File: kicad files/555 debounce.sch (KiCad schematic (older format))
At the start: 7 parts, among them SW1 SW_PUSH_BUTTON

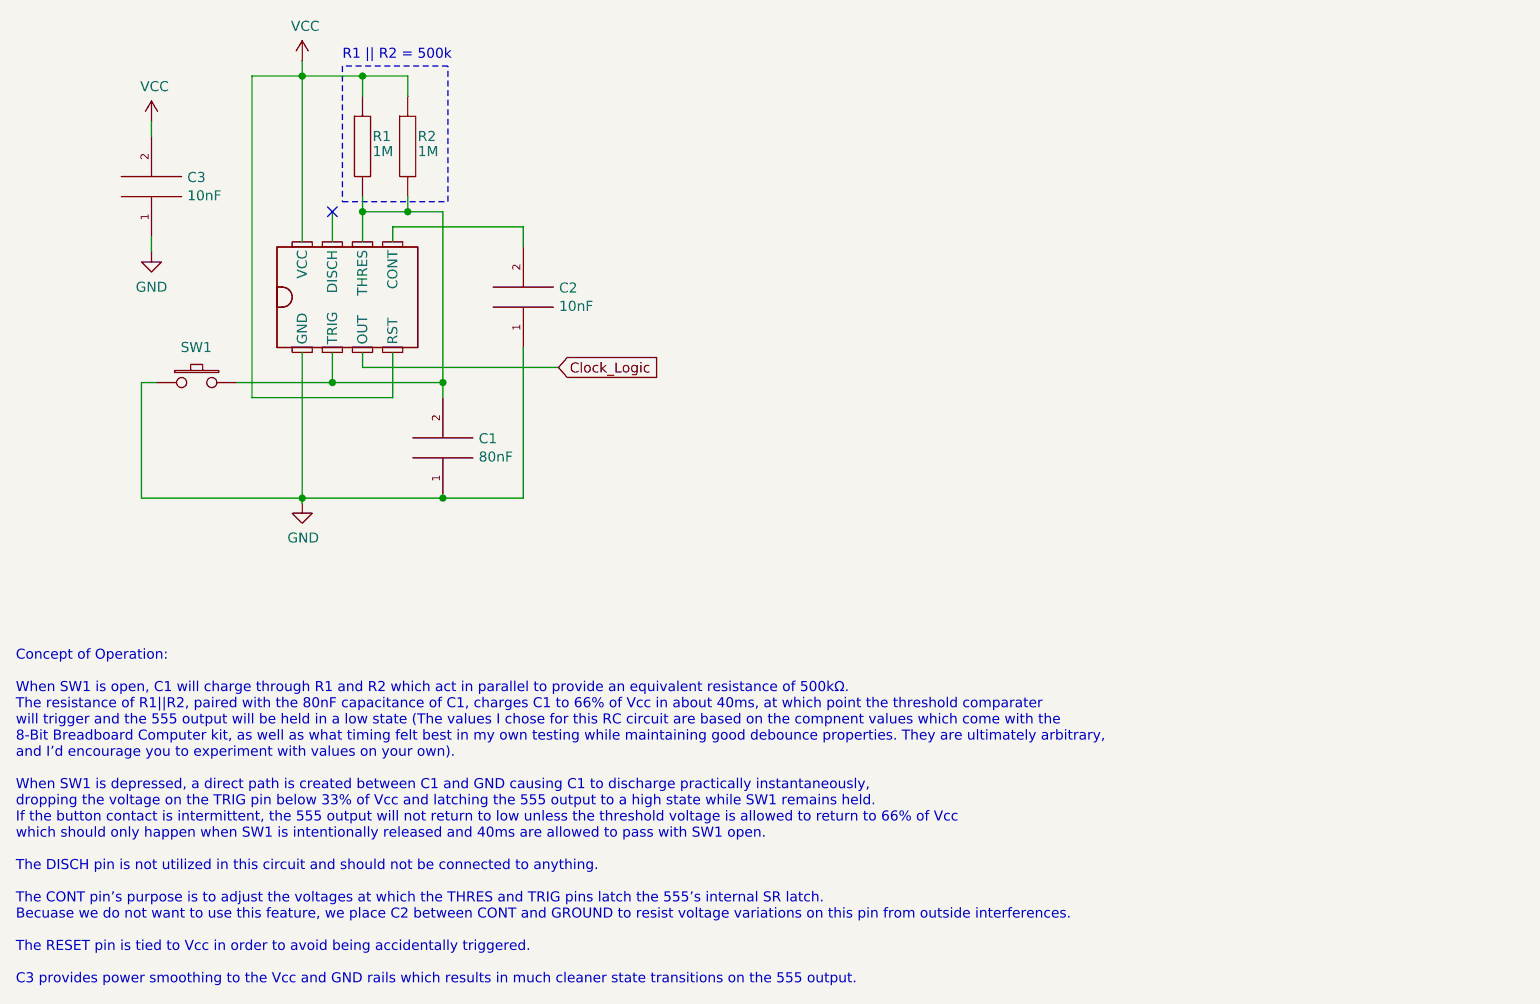
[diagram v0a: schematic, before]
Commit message: corrected C2 value and minor edits
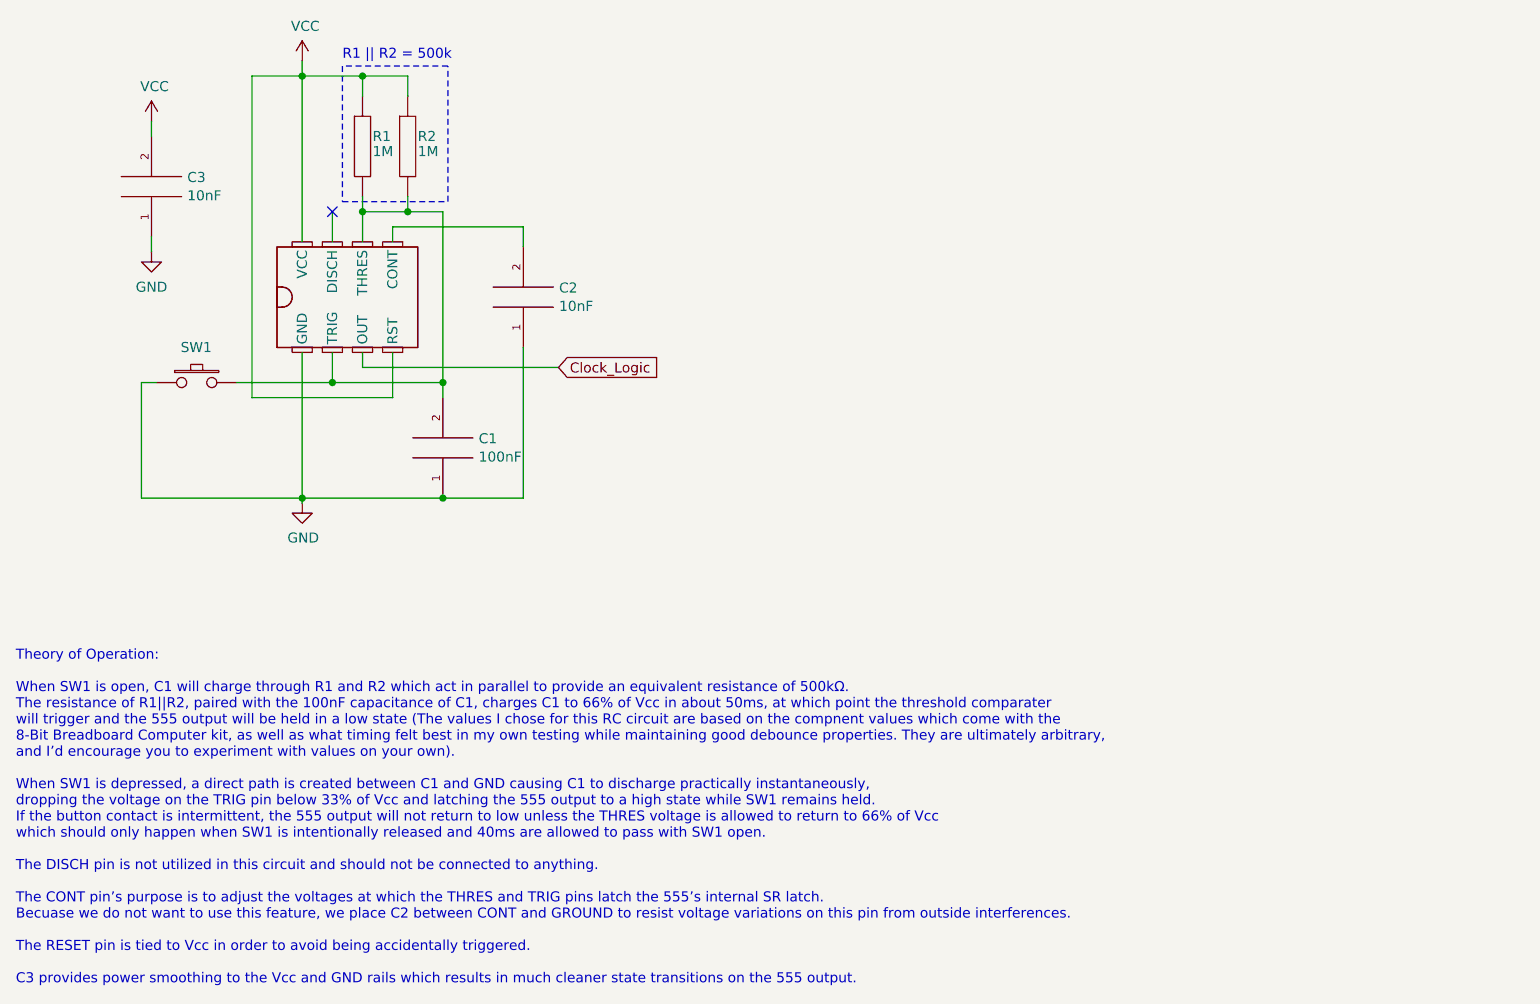
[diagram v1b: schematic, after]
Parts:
- C1: value 80nF -> 100nF
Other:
- note added: "Theory of Operation:\n\nWhen SW1 is open, C1 will charge through R1 and R2 which act in parallel to provide an equivalent resistance of 500kΩ. \nThe resistance of R1||R2, paired with the 100nF capacitance of C1, charges C1 to 66% of Vcc in about 50ms, at which point the threshold comparater \nwill trigger and the 555 output will be held in a low state (The values I chose for this RC circuit are b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"
- note removed: "Concept of Operation:\n\nWhen SW1 is open, C1 will charge through R1 and R2 which act in parallel to provide an equivalent resistance of 500kΩ. \nThe resistance of R1||R2, paired with the 80nF capacitance of C1, charges C1 to 66% of Vcc in about 40ms, at which point the threshold comparater \nwill trigger and the 555 output will be held in a low state (The values I chose for this RC circuit are b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"
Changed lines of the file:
@@
 P 3125 3425
 F 0 "C1" H 2947 3379 50  0000 R CNN
-F 1 "80nF" H 2947 3470 50  0000 R CNN
+F 1 "100nF" H 2947 3470 50  0000 R CNN
 F 2 "" H 3125 3425 50  0001 C CNN
 F 3 "~" H 3125 3425 50  0001 C CNN
@@
 R1 || R2 = 500k
 Text Notes 1000 6100 0    50   ~ 0
-Concept of Operation:\n\nWhen SW1 is open, C1 will charge through R1 and R2 which act in parallel to provide an equivalent resistance of 500kΩ. \nThe resistance of R1||R2, paired with the 80nF capacitance of C1, charges C1 to 66% of Vcc in about 40ms, at which point the threshold comparater \nwill trigger and the 555 output will be held in a low state (The values I chose for this RC circuit are based on the compnent values which come with the\n8-Bit Breadboard Computer kit, as well as what timing felt best in my own testing while maintaining good debounce properties. They are ultimately arbitrary, \nand I’d encourage you to experiment with values on your own).\n\nWhen SW1 is depressed, a direct path is created between C1 and GND causing C1 to discharge practically instantaneously, \ndropping the voltage on the TRIG pin below 33% of Vcc and latching the 555 output to a high state while SW1 remains held. \nIf the button contact is intermittent, the 555 output will not return to low unless the threshold voltage is allowed to return to 66% of Vcc \nwhich should only happen when SW1 is intentionally released and 40ms are allowed to pass with SW1 open.\n\nThe DISCH pin is not utilized in this circuit and should not be connected to anything.\n\nThe CONT pin’s purpose is to adjust the voltages at which the THRES and TRIG pins latch the 555’s internal SR latch. \nBecuase we do not want to use this feature, we place C2 between CONT and GROUND to resist voltage variations on this pin from outside interferences.\n\nThe RESET pin is tied to Vcc in order to avoid being accidentally triggered.\n\nC3 provides power smoothing to the Vcc and GND rails which results in much cleaner state transitions on the 555 output.
+Theory of Operation:\n\nWhen SW1 is open, C1 will charge through R1 and R2 which act in parallel to provide an equivalent resistance of 500kΩ. \nThe resistance of R1||R2, paired with the 100nF capacitance of C1, charges C1 to 66% of Vcc in about 50ms, at which point the threshold comparater \nwill trigger and the 555 output will be held in a low state (The values I chose for this RC circuit are based on the compnent values which come with the\n8-Bit Breadboard Computer kit, as well as what timing felt best in my own testing while maintaining good debounce properties. They are ultimately arbitrary, \nand I’d encourage you to experiment with values on your own).\n\nWhen SW1 is depressed, a direct path is created between C1 and GND causing C1 to discharge practically instantaneously, \ndropping the voltage on the TRIG pin below 33% of Vcc and latching the 555 output to a high state while SW1 remains held. \nIf the button contact is intermittent, the 555 output will not return to low unless the THRES voltage is allowed to return to 66% of Vcc \nwhich should only happen when SW1 is intentionally released and 40ms are allowed to pass with SW1 open.\n\nThe DISCH pin is not utilized in this circuit and should not be connected to anything.\n\nThe CONT pin’s purpose is to adjust the voltages at which the THRES and TRIG pins latch the 555’s internal SR latch. \nBecuase we do not want to use this feature, we place C2 between CONT and GROUND to resist voltage variations on this pin from outside interferences.\n\nThe RESET pin is tied to Vcc in order to avoid being accidentally triggered.\n\nC3 provides power smoothing to the Vcc and GND rails which results in much cleaner state transitions on the 555 output.
 $EndSCHEMATC
